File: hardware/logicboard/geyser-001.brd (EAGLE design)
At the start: 47 x 47 mm, 13 parts, among them T1 2SC1815

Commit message: Refined the board.
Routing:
- net N$9: track 50.3 -> 60.4 mm
- net N$5: track 35.1 -> 44.0 mm, vias 1 -> 0

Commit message: Added silk.
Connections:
- net V12 renamed VIN
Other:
- board text added: "USB"
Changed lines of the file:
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@@
 <text x="24.13" y="2.54" size="0.8128" layer="25" align="bottom-center">VIN=12V -&gt; Connect L&amp;C; VIN=5V -&gt; Connect C&amp;R.</text>
 <text x="6.35" y="43.18" size="0.8128" layer="25">GEYSER 1.0 by Pineapple Computer</text>
+<text x="2.54" y="31.75" size="0.8128" layer="26" rot="R90" align="bottom-center">USB</text>
 </plain>
 <attributes>
@@
 <wire x1="39.37" y1="6.35" x2="36.83" y2="6.35" width="0.127" layer="1"/>
 </signal>
-<signal name="V12">
+<signal name="VIN">
 <contactref element="VOLTAGE-SELECT" pad="3"/>
 <contactref element="U$1" pad="P$20"/>

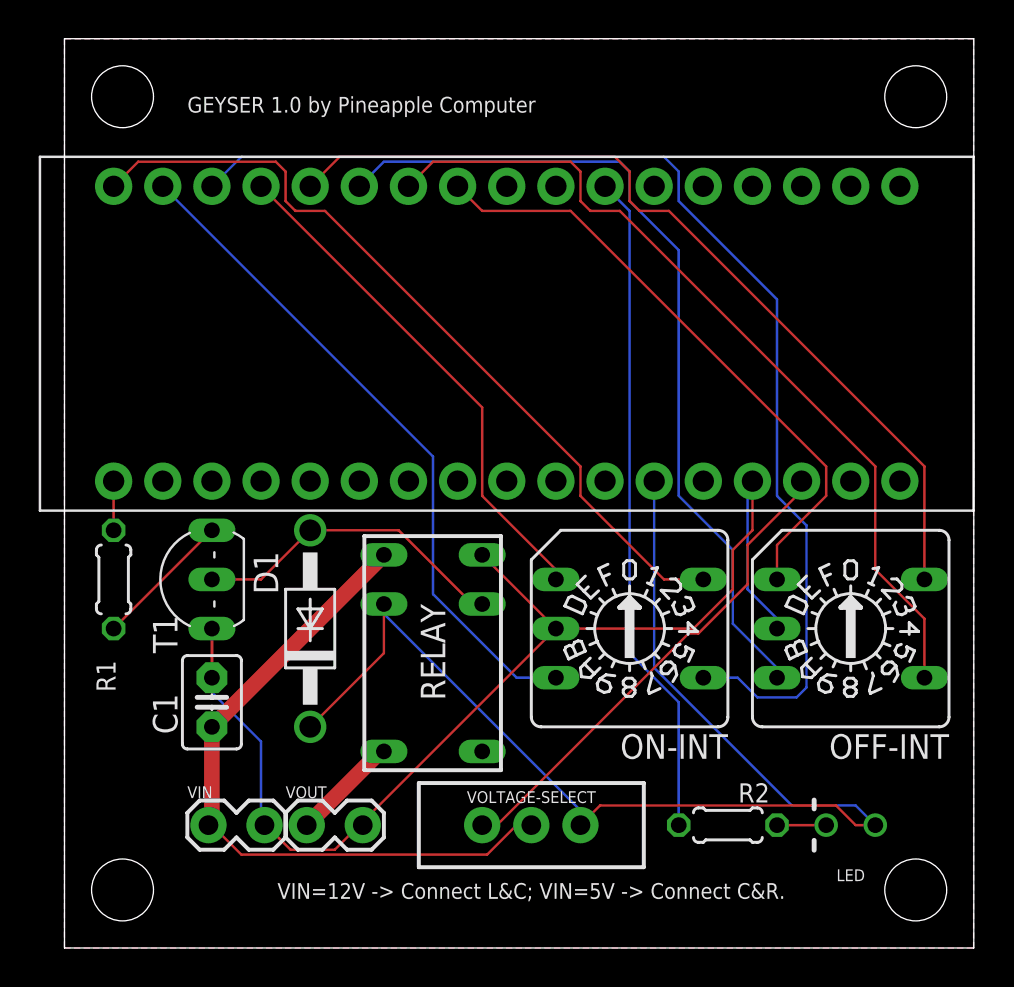
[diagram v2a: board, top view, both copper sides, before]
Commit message: Changed pin layout.
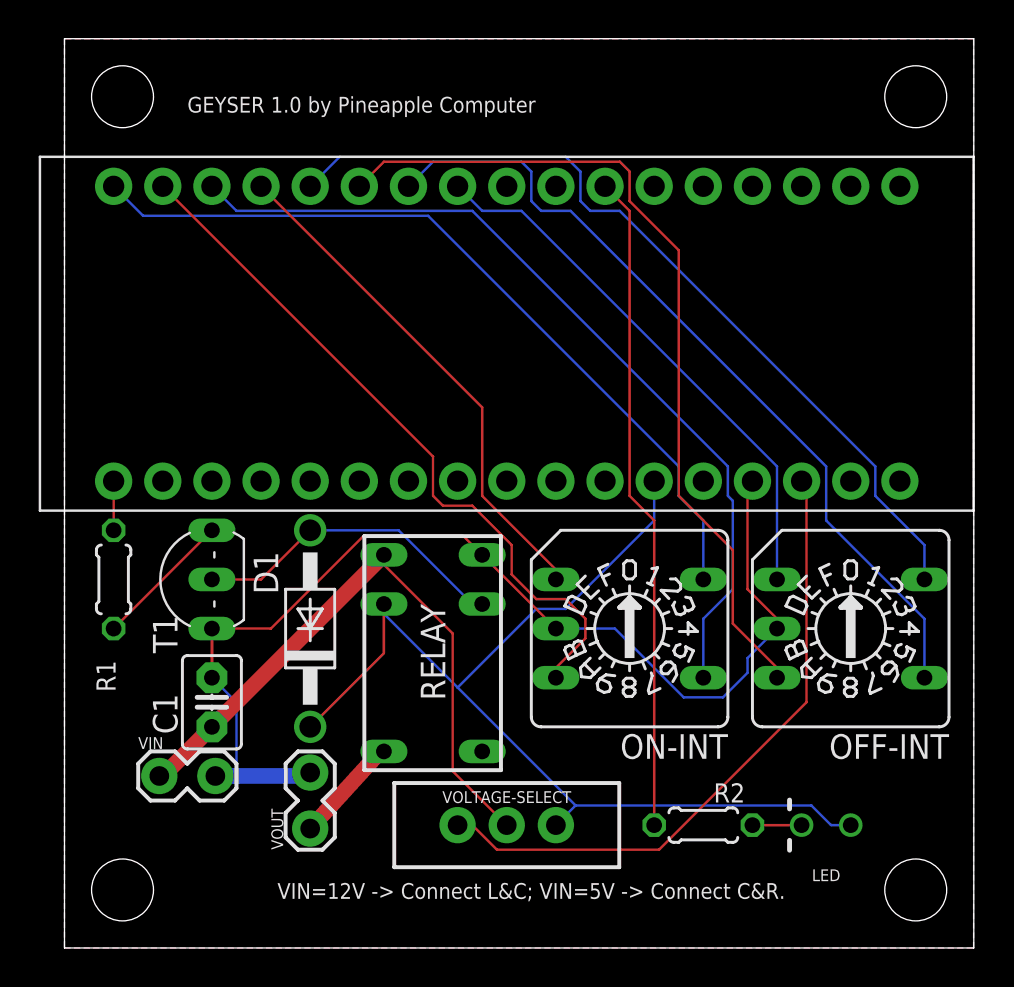
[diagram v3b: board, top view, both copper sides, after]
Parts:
- moved VIN 3.59 mm to (5.08, 8.89)
- moved LED 1.27 mm to (39.4, 6.35)
- moved VOLTAGE-SELECT 1.27 mm to (22.9, 6.35)
- moved R2 1.27 mm to (33.0, 6.35)
- turned VOUT to 90 degrees
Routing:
- net N$9: track 60.4 -> 44.3 mm
- net VCC: track 64.3 -> 54.5 mm
- net VIN: track 25.4 -> 33.3 mm
- net N$11: track 31.9 -> 28.3 mm
- net GND: track 61.6 -> 58.3 mm
- net VDD: track 35.8 -> 33.0 mm
- net N$8: track 35.0 -> 36.9 mm
- net N$6: track 44.0 -> 42.6 mm
- net N$2: track 45.7 -> 44.3 mm
- net LEDDRIVE: track 34.6 -> 34.1 mm

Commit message: Changed copyright notice.
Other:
- board text added: "GEYSER 1.0 by Pineapple Design"
- board text removed: "GEYSER 1.0 by Pineapple Computer"
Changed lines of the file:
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@@
 <hole x="44" y="44" drill="3.2"/>
 <text x="24.13" y="2.54" size="0.8128" layer="25" align="bottom-center">VIN=12V -&gt; Connect L&amp;C; VIN=5V -&gt; Connect C&amp;R.</text>
-<text x="6.35" y="43.18" size="0.8128" layer="25">GEYSER 1.0 by Pineapple Computer</text>
+<text x="6.35" y="43.18" size="0.8128" layer="25">GEYSER 1.0 by Pineapple Design</text>
 <text x="2.54" y="31.75" size="0.8128" layer="26" rot="R90" align="bottom-center">USB</text>
 </plain>

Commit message: Changed layout rule.
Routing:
- net N$9: track 44.3 -> 90.4 mm
- net N$8: track 36.9 -> 69.9 mm, vias 0 -> 2
- net N$10: track 26.6 -> 48.7 mm
- net LEDDRIVE: track 34.1 -> 48.8 mm
- net N$11: track 28.3 -> 42.1 mm
- net N$7: track 41.6 -> 55.2 mm
- net VIN: track 33.3 -> 26.4 mm
- net N$5: track 44.0 -> 49.4 mm, vias 0 -> 1
- net VCC: track 54.5 -> 59.0 mm
- net GND: track 58.3 -> 54.5 mm
- net N$6: track 42.6 -> 45.8 mm, vias 0 -> 1
- net N$2: track 44.3 -> 45.0 mm
- removed copper zone on layer 1, net GND
- removed copper zone on layer 16, net GND
